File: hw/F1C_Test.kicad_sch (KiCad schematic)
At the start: 58 parts, among them J1 USB_C_Receptacle_USB2.0_14P, J2 FPC/FFC P0.5, J3 1x03 P2.54, J4 1x06 P2.54, J5 1x04 P2.54, SW1 SW_Push, SW2 SW_Push, SW3 SW_SPST, U1 ME3103, U2 ME3103, U3 ME3103, U4 F1C100s, U5 W25Q32JVSS, U6 SY7200AABC, Y1 24MHz 20pF

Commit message: hw: Update schematic
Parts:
- removed F1: 1.5A 6V, Fuse:Fuse_1206_3216Metric, symbol Device:Polyfuse
- removed J5: 1x04 P2.54, Connector_PinHeader_2.54mm:PinHeader_1x04_P2.54mm_Vertical, symbol Connector_Generic:Conn_01x04
- added C11, C24, C25: 100n, Capacitor_SMD:C_0402_1005Metric, symbol Device:C
- added J5: AudioJack4, Connector_Audio:Jack_3.5mm_KoreanHropartsElec_PJ-320D-4A_Horizontal, symbol Connector_Audio:AudioJack4
- added R11, R12: 4.7, Resistor_SMD:R_0402_1005Metric, symbol Device:R
- L1, L2: value 2.2u -> 4.7u; footprint Inductor_SMD:L_Sunlord_SWPA252012S -> Inductor_SMD:L_Sunlord_SWPA3015S
- L3: footprint Inductor_SMD:L_Sunlord_SWPA252012S -> Inductor_SMD:L_Sunlord_SWPA3015S
- L4: value 33u -> 4.7u; footprint Inductor_SMD:L_Changjiang_FXL0630 -> Inductor_SMD:L_Sunlord_SWPA3015S
- R3: value 430k -> 110k
- R4: value 130k -> 33k
- U6: value SY7200AABC -> MT9284
- renumbered C11 to C12, C12 to C13, C13 to C14, C14 to C15, C15 to C16, C16 to C17, C17 to C18, C18 to C19, C19 to C20, C20 to C21, C21 to C22, C22 to C23, R11 to R15, R12 to R16
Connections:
- net HP_COMFB is gone; now on net HP_COM: U4.2 (HPCOMFB)
- net +3V3: now also C11.2
- net GND: now also C11.1
- net HP_COM: now also C24.2, C25.2, J5.R2
- net HP_L: now also R11.1
- net HP_R: now also R12.1
- net VBUS: now also C22.1, SW3.1 (A)
- new net: C25.1, J5.R1, R12.2
- new net: C24.1, J5.T, R11.2
- no-connect marks 25 -> 26
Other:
- note added: "21.9 mA"
- note removed: "42.6 mA"
- moved on the sheet: C10, C21, C22, C23, C6, C7, C8, C9, R9, SW3

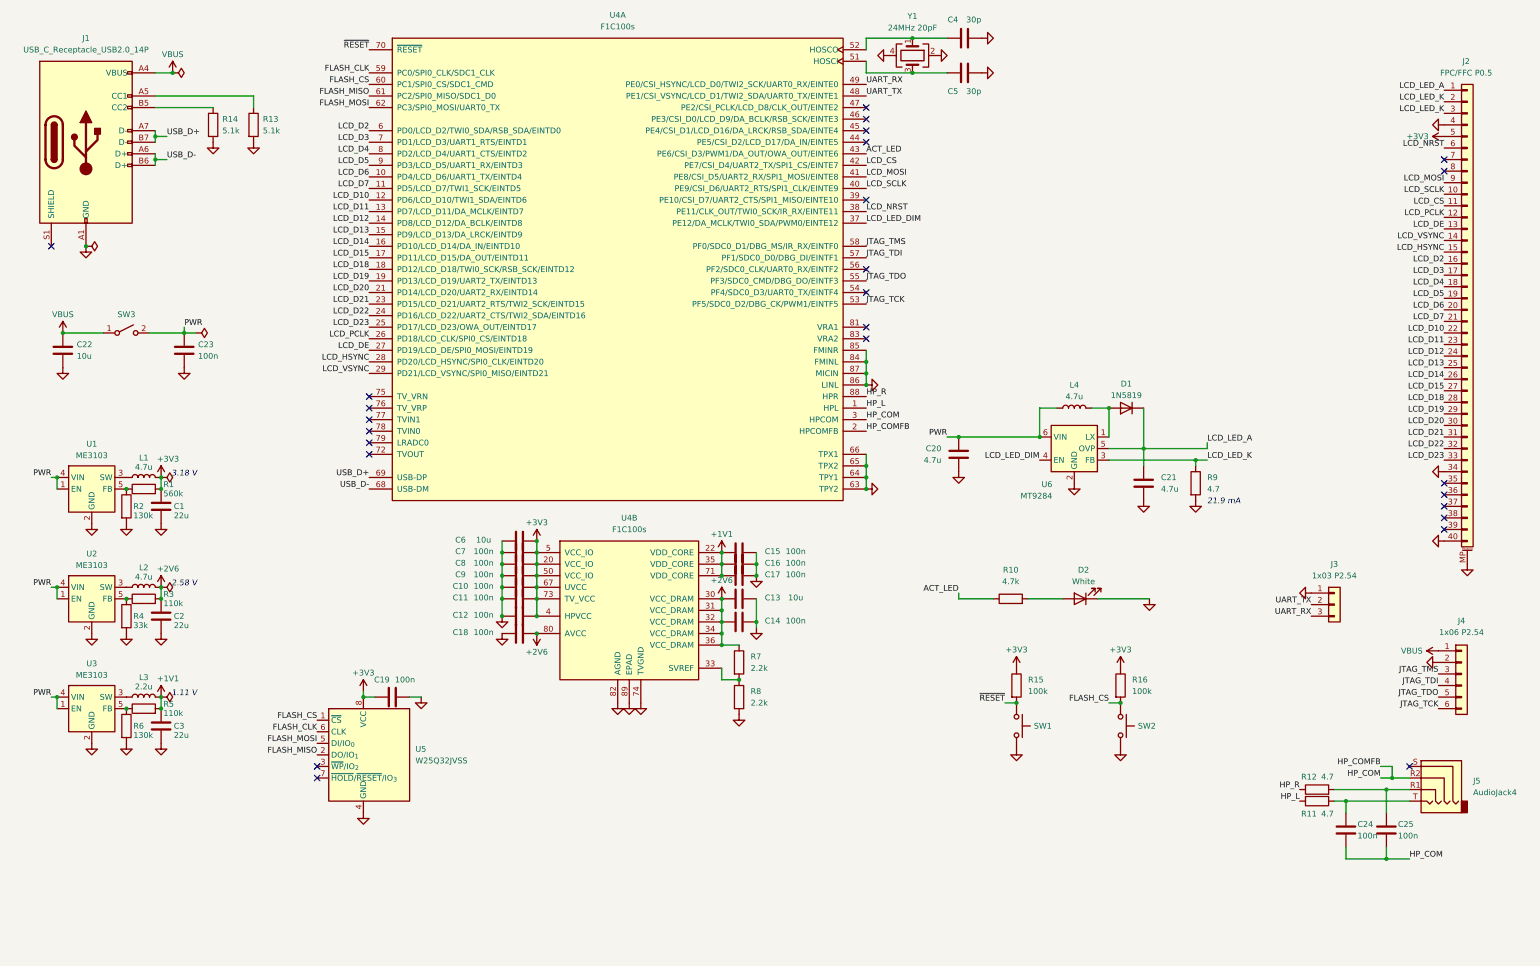
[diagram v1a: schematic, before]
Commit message: hw: Add VRA decoupling networks
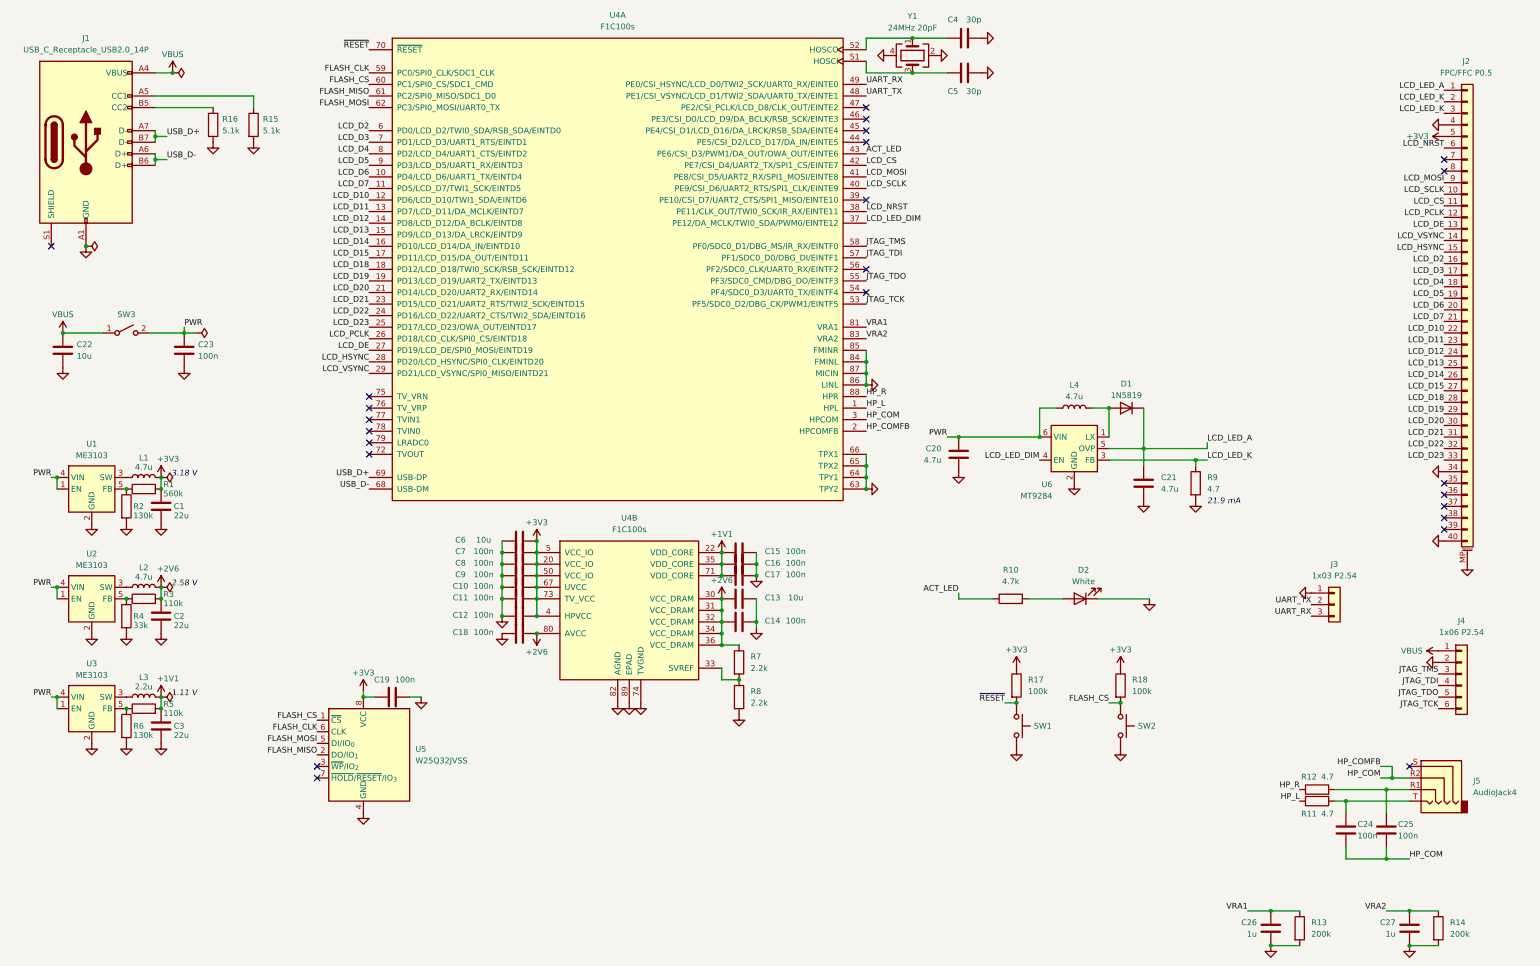
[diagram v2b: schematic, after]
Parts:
- added C26, C27: 1u, Capacitor_SMD:C_0402_1005Metric, symbol Device:C
- added R13, R14: 200k, Resistor_SMD:R_0402_1005Metric, symbol Device:R
- renumbered R13 to R15, R14 to R16, R15 to R17, R16 to R18
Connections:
- net GND: now also C26.2, C27.2, R13.2, R14.2
- net VRA1: now reaches U4.81 (VRA1)
- net VRA1: now also C26.1, R13.1
- net VRA2: now reaches U4.83 (VRA2)
- net VRA2: now also C27.1, R14.1
- no-connect marks 26 -> 24

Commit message: hw: Further incomplete revisions...
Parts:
- J2: footprint FFC_Connector:FPC_1x40_P0.5_L -> FFC_Connector:FPC_1x40_P0.5_R
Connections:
- net LCD_NRST: now also U4.45 (PE4/CSI_D1/LCD_D16/DA_LRCK/RSB_SDA/EINTE4); no longer U4.38 (PE11/CLK_OUT/TWI0_SCK/IR_RX/EINTE11)
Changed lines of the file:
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@@
-	)
-	(no_connect
-		(at 204.47 41.91)
 	)
 	(no_connect
@@
 	)
 	(no_connect
+		(at 204.47 59.69)
+	)
+	(no_connect
 		(at 95.25 102.87)
 	)
@@
 	)
 	(label "LCD_NRST"
-		(at 204.47 59.69 0)
+		(at 204.47 41.91 0)
 		(effects
 			(font
@@
 			)
 		)
-		(property "Footprint" "FFC_Connector:FPC_1x40_P0.5_L"
+		(property "Footprint" "FFC_Connector:FPC_1x40_P0.5_R"
 			(at 336.55 81.28 0)
 			(effects
